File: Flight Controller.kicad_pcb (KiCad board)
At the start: 4 copper layers, 39.5 x 39.5 mm, 123 parts, among them IC1 ICM-20689, IC2 AT7456E, J1 Micro_SD_Card, J2 USB_C_Receptacle_USB2.0_14P, Q1 BC817W, U1 STM32F405RGTx, U2 LMR51430, U3 BMP280, U4 NCP1117-3.3_SOT223

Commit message: Layout Update
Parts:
- moved Rfbb_5R1 19.3 mm to (134.8, 93.5), turned to 180 degrees
- moved Rfbt_5R1 14.3 mm to (134.2, 91.2), turned to 0 degrees
- moved Cin2_5R1 13.0 mm to (139.7, 87.1), turned to -90 degrees
- moved Cin_5R1 12.9 mm to (137.6, 87.1), turned to -90 degrees
- moved Cin3_5R1 12.0 mm to (141.2, 86.3)
- moved C2out_5R1 10.5 mm to (130.1, 82.9), turned to -90 degrees
- moved C1out_5R1 10.3 mm to (128.0, 82.9), turned to -90 degrees
- moved Cboot_5R1 9.77 mm to (132.0, 89.1), turned to 0 degrees
- moved L1 7.42 mm to (134.8, 80.7), turned to 90 degrees
- moved U2 7.19 mm to (134.8, 87.5), turned to -90 degrees
- moved C2_3R1 0.22 mm to (136.5, 74.1)

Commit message: Updated Layout
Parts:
- removed C1_G1: 0.47u, Capacitor_SMD:C_0402_1005Metric
- removed C5: 100n, Capacitor_SMD:C_0402_1005Metric
- removed IC1: ICM-20689, ICM-20689:QFN50P400X400X95-24N
- removed R1, R2: 10k, Resistor_SMD:R_1206_3216Metric
- removed R3_OSD1, R4_OSD1, R5_OSD1: 1k, Resistor_SMD:R_0805_2012Metric
- removed SW_NRST1: SW_Push, Button_Switch_SMD:SW_Tactile_SPST_NO_Straight_CK_PTS636Sx25SMTRLFS
- removed TP_3V1, TP_5V10, TP_5V8, TP_5V9, TP_GND10, TP_GND11, TP_GND12, TP_GND9, TP_Rssi1, TP_S5, TP_S6, TP_VBAT1: TestPoint, Connector:Soldier_Pad
- removed Y_OSD1: 27MHz, Oscillator:Oscillator_SMD_Abracon_ASCO-4Pin_1.6x1.2mm
- added CBOOT_10V1: 0.1u, Capacitor_SMD:C_0402_1005Metric, F.Cu at (202.3, 71.7)
- added CIN_10V1: 4.7u, Capacitor_SMD:C_0805_2012Metric, F.Cu at (203.3, 78.8)
- added CIN_10V2: 4.7u, Capacitor_SMD:C_0805_2012Metric, F.Cu at (203.3, 81.8)
- added CIN_10V3: 0.1u, Capacitor_SMD:C_0402_1005Metric, F.Cu at (202.3, 73.6)
- added COUT_10V1: 22u, Capacitor_SMD:C_0805_2012Metric, F.Cu at (203.3, 84.8)
- added COUT_10V2: 22u, Capacitor_SMD:C_0805_2012Metric, F.Cu at (203.3, 87.9)
- added C_3VG1: 10u, Capacitor_SMD:C_0603_1608Metric_Pad1.08x0.95mm_HandSolder, F.Cu at (203.3, 90.6)
- added C_3VG2: 10u, Capacitor_SMD:C_0603_1608Metric_Pad1.08x0.95mm_HandSolder, F.Cu at (203.3, 93.1)
- added C_VBAT1: 100n, Capacitor_SMD:C_0402_1005Metric, F.Cu at (202.3, 75.6)
- added D6: PESD1CANFD36LS-Q, Diode_SMD:D_SOD-882, F.Cu at (209.6, 75.3)
- added D_LED1: LED, LED_SMD:LED_0603_1608Metric, F.Cu at (207.6, 78.6)
- added D_LED2: LED, LED_SMD:LED_0603_1608Metric, F.Cu at (207.6, 81.2)
- added D_LED3: LED, LED_SMD:LED_0603_1608Metric, F.Cu at (207.6, 83.8)
- added D_LED4: LED, LED_SMD:LED_0603_1608Metric, F.Cu at (207.6, 86.4)
- added L_10V1: 12u, Inductor_SMD:L_Bourns_SRR1208_12.7x12.7mm, F.Cu at (188.6, 70.2)
- added Q2: BC817W, Package_TO_SOT_SMD:SOT-323_SC-70, F.Cu at (206.0, 72.7)
- added RFBB_10V1: 6.2k, Resistor_SMD:R_0805_2012Metric, F.Cu at (183.0, 87.1)
- added RFBT_10V1: 100k, Resistor_SMD:R_1206_3216Metric, F.Cu at (208.3, 89.3)
- added R_BOOT1: 10k, Resistor_SMD:R_0402_1005Metric, F.Cu at (196.1, 85.4)
- added R_BUZ1: 1k, Resistor_SMD:R_0402_1005Metric, F.Cu at (196.1, 87.3)
- added R_CC1: 220, Resistor_SMD:R_0402_1005Metric, F.Cu at (196.1, 89.3)
- added R_FLASH1: 10K, Resistor_SMD:R_0402_1005Metric, F.Cu at (196.1, 91.3)
- added R_FLASH2: 10K, Resistor_SMD:R_0402_1005Metric, F.Cu at (196.1, 93.3)
- added R_LED1: 1k, Resistor_SMD:R_0603_1608Metric, F.Cu at (192.6, 85.6)
- added R_LED2: 1k, Resistor_SMD:R_0603_1608Metric, F.Cu at (192.6, 88.1)
- added R_LED3: 1k, Resistor_SMD:R_0603_1608Metric, F.Cu at (192.6, 90.6)
- added R_LED4: 1k, Resistor_SMD:R_0603_1608Metric, F.Cu at (192.6, 93.2)
- added R_VBAT1: 100K, Resistor_SMD:R_0805_2012Metric, F.Cu at (183.0, 90.1)
- added R_VBAT2: 10K, Resistor_SMD:R_1206_3216Metric, F.Cu at (208.3, 92.7)
- added TP_VBAT+2: TestPoint, TestPoint:TestPoint_Pad_D2.5mm, F.Cu at (198.6, 73.0)
- added U5: LMR51430, Package_TO_SOT_SMD:SOT-23-6, F.Cu at (187.7, 88.0)
- added U6: W25Q128JVSIQ TR, footprints:SOIC_208MIL_WIN, F.Cu at (195.8, 80.8)
- added U7: ICM-42688-P, Package_LGA:Bosch_LGA-14_3x2.5mm_P0.5mm, F.Cu at (187.7, 92.5)
- added U8: NCP1117-3.3_SOT223, Package_TO_SOT_SMD:SOT-223-3_TabPin2, F.Cu at (185.7, 81.5)
- added Y2: 27M, AWSCR-27.00CV-T :E2X270061X04, F.Cu at (210.1, 72.4)
- C_3V1: renamed from C1_3R1; footprint Capacitor_SMD:C_0805_2012Metric -> Capacitor_SMD:C_0603_1608Metric
- C_3V2: renamed from C2_3R1; footprint Capacitor_SMD:C_0805_2012Metric -> Capacitor_SMD:C_0603_1608Metric
- C_DEC1: renamed from C1_Dec1; footprint Capacitor_SMD:C_0805_2012Metric -> Capacitor_SMD:C_0603_1608Metric
- C_GYRO1: renamed from C3_G1; footprint Capacitor_SMD:C_0805_2012Metric -> Capacitor_SMD:C_0402_1005Metric
- C_OSD2: renamed from C2_OSD1; footprint Capacitor_SMD:C_0805_2012Metric -> Capacitor_SMD:C_0402_1005Metric
- C_OSD3: renamed from C3_OSD1; footprint Capacitor_SMD:C_0805_2012Metric -> Capacitor_SMD:C_0402_1005Metric
- D_LED5: renamed from D1_LED1; footprint LED_SMD:LED_0402_1005Metric -> LED_SMD:LED_0603_1608Metric
- D_LED6: renamed from D2_LED1; footprint LED_SMD:LED_0402_1005Metric -> LED_SMD:LED_0603_1608Metric
- IC2: footprint MAX7456EUI:SOP65P637X110-28N -> max74:SOP65P637X110-28N
- J1: value Micro_SD_Card -> Conn_01x08_MountingPin; footprint Connector_Card:microSD_HC_Molex_47219-2001 -> Connector_JST:JST_SH_SM08B-SRSS-TB_1x08-1MP_P1.00mm_Horizontal; moved to F.Cu
- J2: footprint Connector_USB:USB_C_Receptacle_HRO_TYPE-C-31-M-12 -> Connector_USB:USB_C_Receptacle_GCT_USB4110
- JP1: value SolderJumper_3_Open -> Jumper_3
- L_5V1: renamed from L1; value 6.8u -> 8.2u; footprint Inductor_SMD:L_Abracon_ASPI-0630LR -> Inductor_SMD:L_Vishay_IHLP-2525
- R_I2C1: renamed from R3_I2C1; footprint Resistor_SMD:R_0603_1608Metric -> Resistor_SMD:R_0402_1005Metric
- R_I2C2: renamed from R3_I2C2; footprint Resistor_SMD:R_0603_1608Metric -> Resistor_SMD:R_0402_1005Metric
- R_LED5: renamed from R1_LED1; footprint Resistor_SMD:R_0805_2012Metric -> Resistor_SMD:R_0603_1608Metric
- R_LED6: renamed from R2_LED1; footprint Resistor_SMD:R_0805_2012Metric -> Resistor_SMD:R_0603_1608Metric
- R_SBUS2: renamed from R1_SBUS1; footprint Resistor_SMD:R_1206_3216Metric -> Resistor_SMD:R_0603_1608Metric
- U1: value STM32F405RGTx -> AT32F435RGT7
- Y1: renamed from 8M1; value Resonator -> 8M
- moved J1 65.4 mm to (202.8, 66.9), turned to 0 degrees
- renumbered Cboot_5R1 to CBOOT_5V1, Cin_5R1 to CIN_5V1, Cin2_5R1 to CIN_5V2, Cin3_5R1 to CIN_5V3, C1out_5R1 to COUT_5V1, C2out_5R1 to COUT_5V2, C3 to C_BARO1, C4 to C_BARO2, C2_Dec1 to C_DEC2, C3_Dec1 to C_DEC3, C4_Dec1 to C_DEC4, C5_Dec1 to C_DEC5, C6_Dec1 to C_DEC6, C7_Dec1 to C_DEC7, C4_G1 to C_GYRO2, C2_G1 to C_GYRO3, C1_OSD1 to C_OSD1, C4_OSD1 to C_OSD4, C5_OSD1 to C_OSD5, C6_OSD1 to C_OSD6, Q1 to Q_SBUS1, Rfbb_5R1 to RFBB_5V1, Rfbt_5R1 to RFBT_5V1, R1_OSD1 to R_OSD1, R2_OSD1 to R_OSD2, R2_SBUS1 to R_SBUS1, R4_USB2 to R_USB1, R3_USB2 to R_USB2, TP_SBUS1 to TP_RX1, TP_TX1 to TP_SBUS1
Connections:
- net Net-(U1-PH0) renamed /RES1
- net Net-(U1-PH1) renamed /RES2
- net Net-(U1-VCAP_1) renamed /CAP1
- net Net-(U1-VCAP_2) renamed /CAP2
- net Net-(U4-VI) renamed /5V_OUT
- CIN_5V1 pad 2: Net-(U2-GND) -> GND
- CIN_5V2 pad 2: Net-(U2-GND) -> GND
- CIN_5V3 pad 1: Net-(U2-GND) -> GND
- COUT_5V1 pad 2: Net-(U2-GND) -> GND
- COUT_5V2 pad 2: Net-(U2-GND) -> GND
- C_GYRO3 pad 1: +3.3V -> +3.3V_GYRO
- IC2 pad 10: /SPI2_SCLK -> /OSD_SCLK
- IC2 pad 11: /SPI2_MISO -> /OSD_MISO
- IC2 pad 12: /LOS -> unconnected-(IC2-LOS-Pad12)
- IC2 pad 17: /VS -> unconnected-(IC2-~{VSYNC}-Pad17)
- IC2 pad 18: /HS -> unconnected-(IC2-~{HSYNC}-Pad18)
- IC2 pad 7: /CLKOUT -> unconnected-(IC2-CLKOUT-Pad7)
- IC2 pad 9: /SPI2_MOSI -> /OSD_MOSI
- J1 pad 1: unconnected-(J1-DAT2-Pad1) -> /VBAT+
- J1 pad 2: /SD_CS -> GND
- J1 pad 3: /SPI2_MOSI -> /S1
- J1 pad 4: +3.3V -> /S2
- J1 pad 5: /SPI2_SCLK -> /S3
- J1 pad 6: GND -> /S4
- J1 pad 7: /SPI2_MISO -> /ADC_Curr
- J1 pad 8: unconnected-(J1-DAT1-Pad8) -> /TEL
- RFBB_5V1 pad 2: Net-(U2-GND) -> GND
- R_I2C1 pad 2: /I2C_SDA -> /I2C2_SDA
- R_I2C2 pad 1: /I2C_SCL -> /I2C2_SCL
- R_LED5 pad 2: /LED1 -> /LED0
- R_LED6 pad 2: /LED2 -> /LED1
- TP_Buz1 pad 1: /Buz -> /BUZ-
- TP_Curr1 pad 1: /Curr -> /ADC_Curr
- TP_GND5 pad 1: GND -> +5V
- TP_LED1 pad 1: /LED_Out -> /LED_S
- TP_S2 pad 1: /S2 -> /S3
- TP_S3 pad 1: /S3 -> /S2
- TP_SCL1 pad 1: /I2C_SCL -> /I2C2_SCL
- TP_SDA1 pad 1: /I2C_SDA -> /I2C2_SDA
- U1 pad 10: /SPI2_MISO -> unconnected-(U1-PC2-Pad10)
- U1 pad 11: /SPI2_MOSI -> /ADC_Curr
- U1 pad 14: /Curr -> /UART4_TX
- U1 pad 15: /Rssi -> /UART4_RX
- U1 pad 2: unconnected-(U1-PC13-Pad2) -> /BUZ
- U1 pad 20: /VBAT+ -> /GYRO_CS
- U1 pad 21: /SPI1_SCLK -> /OSD_SCLK
- U1 pad 22: /SPI1_MISO -> /OSD_MISO
- U1 pad 23: /SPI1_MOSI -> /OSD_MOSI
- U1 pad 24: /INT -> /GYRO_INT
- U1 pad 25: Net-(U1-PC5) -> unconnected-(U1-PC5-Pad25)
- U1 pad 26: /OSD_CS -> /LED0
- U1 pad 27: /SD_CS -> /LED1
- U1 pad 29: /UART3_TX -> /I2C2_SCL
- U1 pad 30: /UART3_RX -> /I2C2_SDA
- U1 pad 33: unconnected-(U1-PB12-Pad33) -> /FLASH_CS
- U1 pad 34: /SPI2_SCLK -> /GYRO_SCLK
- U1 pad 35: unconnected-(U1-PB14-Pad35) -> /GYRO_MISO
- U1 pad 36: unconnected-(U1-PB15-Pad36) -> /GYRO_MOSI
- U1 pad 37: /S3 -> /S1
- U1 pad 38: /S4 -> /S2
- U1 pad 39: /S5 -> /S3
- U1 pad 40: /S6 -> /S4
- U1 pad 41: /S1 -> /LED_S
- U1 pad 42: /S2 -> /CC
- U1 pad 43: /UART1_RX -> unconnected-(U1-PA10-Pad43)
- U1 pad 46: unconnected-(U1-PA13-Pad46) -> /SWD
- U1 pad 49: unconnected-(U1-PA14-Pad49) -> /SWC
- U1 pad 50: /Buz -> /OSD_CS
- U1 pad 51: /UART4_TX -> /UART3_TX
- U1 pad 52: /UART4_RX -> /UART3_RX
- U1 pad 55: /LED_Out -> /FLASH_SCLK
- U1 pad 56: /LED1 -> /FLASH_MISO
- U1 pad 57: /LED2 -> /FLASH_MOSI
- U1 pad 59: /I2C_SDA -> /UART1_RX
- U1 pad 60: Net-(JP1-C) -> /BOOT
- U1 pad 61: /I2C_SCL -> /BARO_SCL
- U1 pad 62: unconnected-(U1-PB9-Pad62) -> /BARO_SDA
- U1 pad 7: Net-(U1-NRST) -> unconnected-(U1-NRST-Pad7)
- U1 pad 8: /Baro_CS -> unconnected-(U1-PC0-Pad8)
- U1 pad 9: /Gyro_CS -> /ADC_VBAT
- U2 pad 1: Net-(U2-GND) -> GND
- U3 pad 2: /Baro_CS -> +3.3V
- U3 pad 3: /SPI1_MOSI -> /BARO_SDA
- U3 pad 4: /SPI1_SCLK -> /BARO_SCL
- U3 pad 5: /SPI1_MISO -> GND

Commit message: First Layout
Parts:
- CBOOT_10V1, CBOOT_5V1: footprint Capacitor_SMD:C_0402_1005Metric -> Capacitor_SMD:C_0603_1608Metric
- C_3VG1, C_3VG2, J1, R_FLASH1, R_FLASH2, R_LED1, R_LED2, R_LED3, R_LED4, R_LED5, R_LED6, U6, U8, Y2: moved to B.Cu
- L_10V1: footprint Inductor_SMD:L_Bourns_SRR1208_12.7x12.7mm -> Wurth-Elektronik:744393465120
- RFBB_10V1, RFBB_5V1: footprint Resistor_SMD:R_0805_2012Metric -> Resistor_SMD:R_0402_1005Metric
- RFBT_10V1, RFBT_5V1: footprint Resistor_SMD:R_1206_3216Metric -> Resistor_SMD:R_0402_1005Metric
- moved D_LED4 73.1 mm to (134.5, 83.5), turned to 180 degrees
- moved D_LED3 73.1 mm to (134.5, 81.8), turned to 180 degrees
- moved D_LED2 73.1 mm to (134.5, 80.0), turned to 180 degrees
- moved D_LED1 73.0 mm to (134.5, 78.2), turned to 180 degrees
- moved COUT_10V1 73.0 mm to (130.3, 85.8)
- moved COUT_10V2 73.0 mm to (130.3, 87.8)
- moved CIN_10V3 70.9 mm to (135.2, 96.7), turned to 180 degrees
- moved RFBT_10V1 69.3 mm to (139.0, 90.6), turned to -90 degrees
- moved CIN_10V1 68.9 mm to (135.8, 92.9)
- moved CIN_10V2 68.8 mm to (135.8, 95.0)
- moved J1 68.0 mm to (144.2, 101.5), turned to 180 degrees
- moved CBOOT_10V1 67.3 mm to (136.9, 87.5), turned to 180 degrees
- moved R_FLASH1 66.3 mm to (133.7, 69.0), turned to -90 degrees
- moved Y2 64.0 mm to (151.0, 96.9), turned to 180 degrees
- moved R_LED4 63.2 mm to (130.2, 83.5)
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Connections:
- D2 pad 1: +5V -> /5V_USB
- D2 pad 2: /5V_USB -> +5V

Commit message: Updated Layout
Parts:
- removed TP_3V2, TP_5V1, TP_5V11, TP_5V12, TP_5V2, TP_5V3, TP_5V4, TP_5V5, TP_5V6, TP_5V7, TP_Buz1, TP_CAM1, TP_Curr1, TP_GND1, TP_GND2, TP_GND3, TP_GND4, TP_LED1, TP_VTX1: TestPoint, Connector:Soldier_Pad
- removed TP_VBAT-1: TestPoint, TestPoint:TestPoint_Pad_D2.5mm
- added 10V: TestPoint, Pads:Solder_Pad_SMD, F.Cu at (134.6, 99.3)
- added 3V: TestPoint, Pads:Solder_Pad_SMD, F.Cu at (136.5, 99.3)
- added 3V: TestPoint, Pads:Solder_Pad_SMD, F.Cu at (138.4, 99.3)
- added 5V: TestPoint, Pads:Solder_Pad_SMD, F.Cu at (147.9, 99.3)
- added 5V: TestPoint, Pads:Solder_Pad_SMD, F.Cu at (144.1, 99.3)
- added 5V: TestPoint, Pads:Solder_Pad_SMD, F.Cu at (149.8, 99.3)
- added 5V: TestPoint, Pads:Solder_Pad_SMD, F.Cu at (134.9, 124.8)
- added 5V: TestPoint, Pads:Solder_Pad_SMD, F.Cu at (140.3, 99.3)
- added 5V: TestPoint, Pads:Solder_Pad_SMD, F.Cu at (137.5, 102.9)
- added 5V: TestPoint, Pads:Solder_Pad_SMD, F.Cu at (142.2, 99.3)
- added 5V: TestPoint, Pads:Solder_Pad_SMD, F.Cu at (151.7, 99.3)
- added 5V: TestPoint, Pads:Solder_Pad_SMD, F.Cu at (135.6, 102.9)
- added 5V: TestPoint, Pads:Solder_Pad_SMD, F.Cu at (146.0, 99.3)
- added Buz: TestPoint, Pads:Solder_Pad_SMD, F.Cu at (139.4, 102.9)
- added CAM: TestPoint, Pads:Solder_Pad_SMD, F.Cu at (141.3, 102.9)
- added CC: TestPoint, Pads:Solder_Pad_SMD, F.Cu at (143.2, 102.9)
- added Curr: TestPoint, Pads:Solder_Pad_SMD, F.Cu at (145.1, 102.9)
- added G***: LOGO, Pads:OpenSource_Logo, F.Cu at (141.3, 94.9)
- added G***: LOGO, Pads:FAFO_LOGO, F.Cu at (160.1, 95.3)
- added G***: LOGO, Pads:OpenSource_Text, F.Cu at (147.6, 95.7)
- added GND: TestPoint, Pads:Solder_Pad_SMD, F.Cu at (147.0, 102.9)
- added GND: TestPoint, Pads:Solder_Pad_SMD, F.Cu at (153.6, 99.3)
- added GND: TestPoint, Pads:Solder_Pad_SMD, F.Cu at (150.8, 102.9)
- added GND: TestPoint, Pads:Solder_Pad_SMD, F.Cu at (148.9, 102.9)
- added LED: TestPoint, Pads:Solder_Pad_SMD, F.Cu at (152.7, 102.9)
- added TEL: TestPoint, Pads:Solder_Pad_SMD, F.Cu at (154.6, 102.9)
- added TP_GND10: TestPoint, Pads:Solder_Pad_SMD, F.Cu at (143.3, 67.5)
- added TP_GND15: TestPoint, Pads:Solder_Pad_SMD, F.Cu at (149.0, 67.5)
- added TP_GND9: TestPoint, Pads:Solder_Pad_SMD, F.Cu at (141.4, 67.5)
- added TP_S5: TestPoint, Pads:Solder_Pad_SMD, F.Cu at (150.9, 67.5)
- added TP_S6: TestPoint, Pads:Solder_Pad_SMD, F.Cu at (152.8, 67.5)
- added TP_S7: TestPoint, Pads:Solder_Pad_SMD, F.Cu at (146.5, 133.0)
- added TP_S8: TestPoint, Pads:Solder_Pad_SMD, F.Cu at (148.4, 133.0)
- added TP_SWC1: TestPoint, Pads:Solder_Pad_SMD, F.Cu at (174.4, 129.3)
- added TP_SWD1: TestPoint, Pads:Solder_Pad_SMD, F.Cu at (154.7, 67.5)
- added TP_TX1: TestPoint, Pads:Solder_Pad_SMD, F.Cu at (151.8, 71.0)
- added VBAT: TestPoint, Pads:Solder_Pad_SMD, F.Cu at (161.2, 126.4)
- added VTX: TestPoint, Pads:Solder_Pad_SMD, F.Cu at (155.5, 99.3)
- C_DEC1, D6: moved to B.Cu
- FC 1: renamed from D_LED5
- FC 2: renamed from D_LED6
- TP_GND13, TP_GND14, TP_GND5, TP_GND6, TP_GND7, TP_GND8, TP_RX1, TP_RX2, TP_RX3, TP_RX4, TP_RX5, TP_S1, TP_S2, TP_S3, TP_S4, TP_SBUS1, TP_SCL1, TP_SDA1, TP_TX2, TP_TX3, TP_TX4, TP_TX5: footprint Connector:Soldier_Pad -> Pads:Solder_Pad_SMD
- TP_VBAT+1, TP_VBAT+2: footprint TestPoint:TestPoint_Pad_D2.5mm -> Pads:Solder_Pad_SMD
- moved TP_SBUS1 159.8 mm to (150.3, 133.0)
- moved TP_TX4 153.9 mm to (148.4, 136.8)
- moved TP_GND5 153.3 mm to (145.6, 126.7)
- moved TP_TX3 147.6 mm to (146.5, 136.8)
- moved TP_SDA1 137.7 mm to (155.6, 71.0)
- moved TP_S4 127.0 mm to (149.9, 71.0)
- moved TP_GND6 124.7 mm to (135.7, 67.5)
- moved TP_TX2 121.2 mm to (153.7, 71.0)
- moved TP_GND13 119.7 mm to (145.2, 67.5)
- moved TP_S1 118.9 mm to (144.2, 71.0)
- moved TP_GND14 118.6 mm to (147.1, 67.5)
- moved TP_S2 115.9 mm to (146.1, 71.0)
- moved TP_S3 111.8 mm to (148.0, 71.0)
- moved R_BUZ1 110.2 mm to (135.3, 75.0), turned to 90 degrees
- moved Q2 109.2 mm to (137.8, 74.0)
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- renumbered D_LED2 to 10V, D_LED3 to 3.3V, D_LED1 to 5V, D_LED4 to Gyro

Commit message: Updated Layout
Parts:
- removed 10V, 3V (x2), 5V (x10), Buz, CAM, CC, Curr, GND (x4), LED, TEL, TP_GND10, TP_GND13, TP_GND14, TP_GND15, TP_GND5, TP_GND6, TP_GND7, TP_GND8, TP_GND9, TP_RX1, TP_RX2, TP_RX3, TP_RX4, TP_RX5, TP_S1, TP_S2, TP_S3, TP_S4, TP_S5, TP_S6, TP_S7, TP_S8, TP_SBUS1, TP_SCL1, TP_SDA1, TP_SWC1, TP_SWD1, TP_TX1, TP_TX2, TP_TX3, TP_TX4, TP_TX5, TP_VBAT+1, TP_VBAT+2, VBAT, VTX: TestPoint, Pads:Solder_Pad_SMD
- D_LED5: renamed from FC 1
- D_LED6: renamed from FC 2
- moved R_I2C1 17.4 mm to (148.5, 93.5), turned to 90 degrees
- moved R_I2C2 17.3 mm to (147.4, 93.5), turned to -90 degrees
- moved R_VBAT1 12.4 mm to (138.8, 94.1), turned to -90 degrees
- moved R_VBAT2 12.1 mm to (141.0, 94.7), turned to -90 degrees
- moved C_VBAT1 11.9 mm to (142.7, 95.5), turned to 90 degrees
- moved D2 4.47 mm to (146.3, 82.8)
- moved R_USB2 2.15 mm to (158.6, 75.9)
- moved C_DEC6 1.93 mm to (138.3, 80.2)
- moved C_DEC7 1.93 mm to (154.5, 80.9), turned to 0 degrees
- moved C1 1.70 mm to (149.9, 92.9)
- moved R_LED1 1.48 mm to (128.7, 78.0)
- moved R_LED2 1.48 mm to (128.7, 79.8)
- moved R_LED3 1.48 mm to (128.7, 81.5)
- moved R_LED4 1.48 mm to (128.7, 83.2)
- moved R_LED5 1.48 mm to (128.7, 74.5)
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- renumbered 5V to D_LED1, 10V to D_LED2, 3.3V to D_LED3, Gyro to D_LED4
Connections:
- U1 pad 26: /LED0 -> /LED1
- U1 pad 27: /LED1 -> /LED0

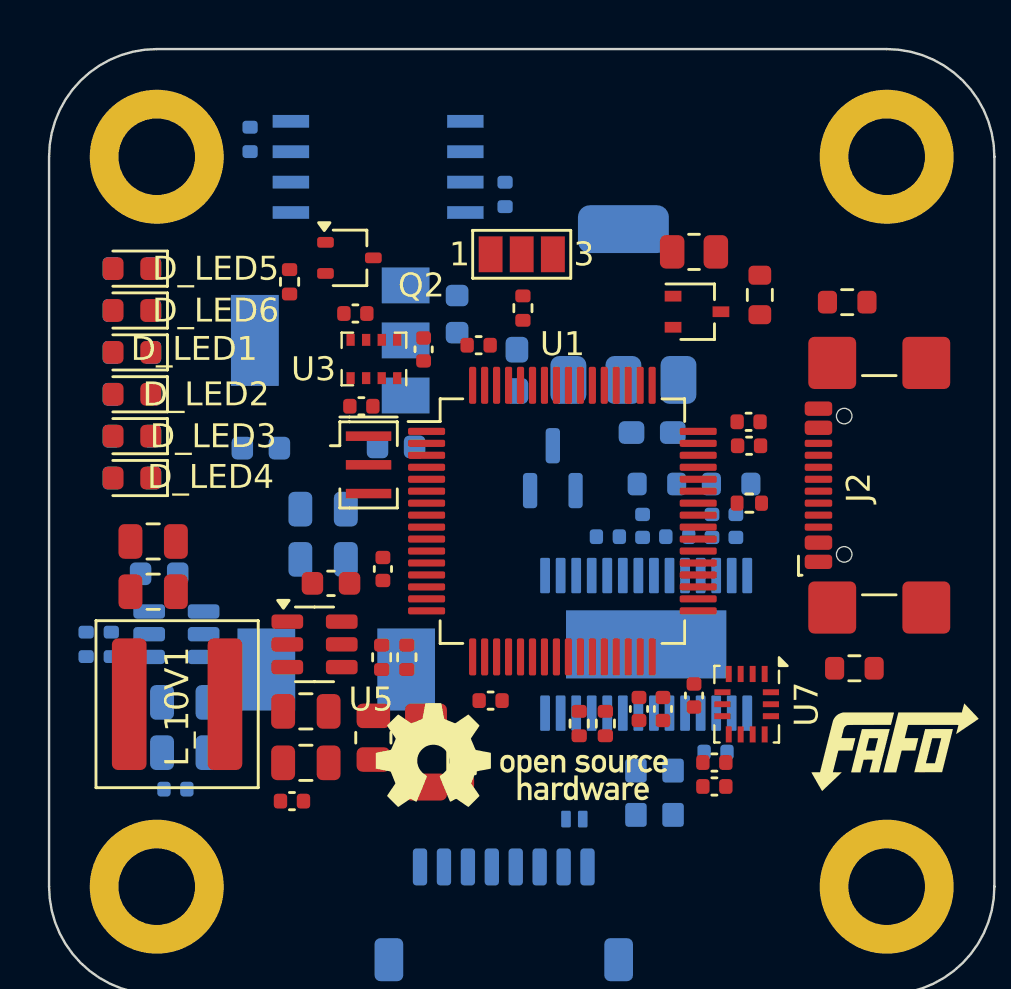
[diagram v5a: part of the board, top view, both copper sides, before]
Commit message: Changed LDOs
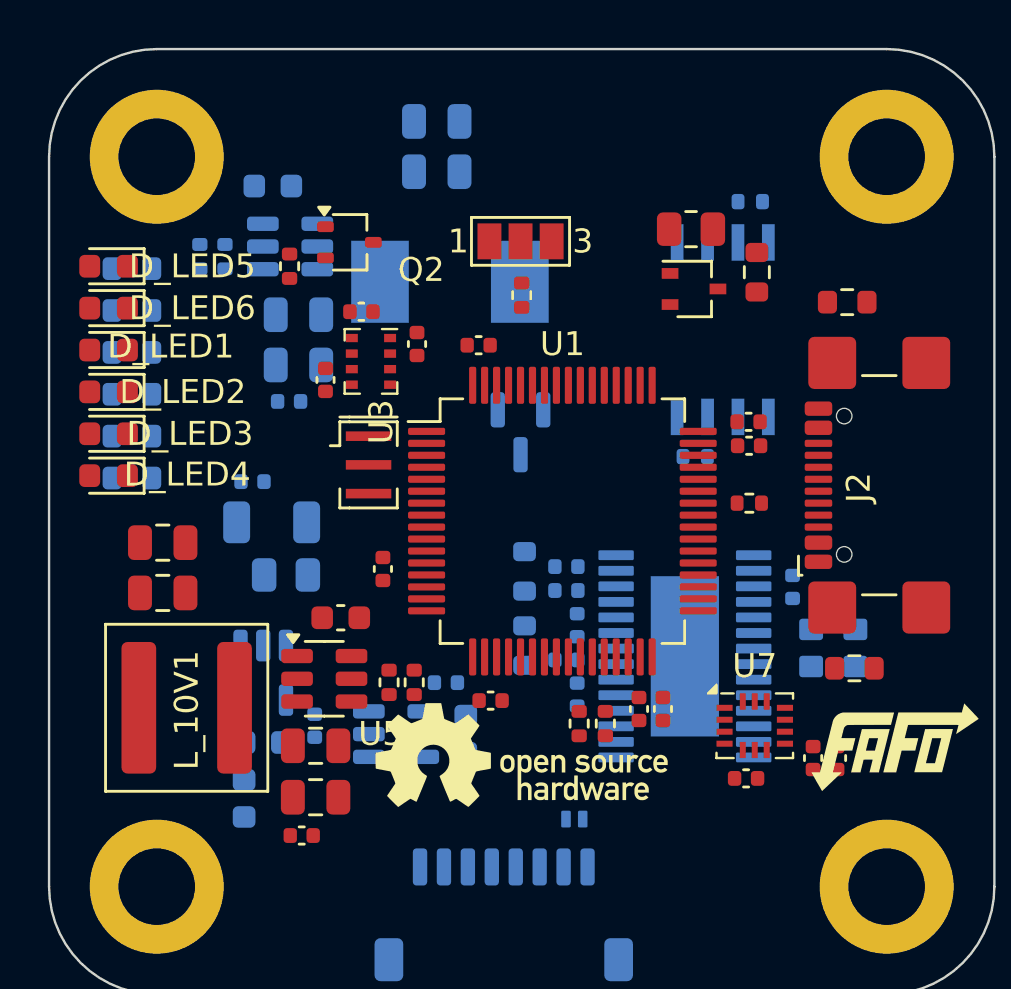
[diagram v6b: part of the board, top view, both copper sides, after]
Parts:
- removed the C_3VG1 at (144.8, 78.8)
- added C_3VG2: 10n, Capacitor_SMD:C_0402_1005Metric, B.Cu at (141.8, 91.8)
- C_3V1: value 10u -> 1u
- C_3V2: value 10u -> 10n; footprint Capacitor_SMD:C_0603_1608Metric -> Capacitor_SMD:C_0402_1005Metric
- C_3VG1: renamed from C_3VG2; value 10u -> 1u; footprint Capacitor_SMD:C_0603_1608Metric_Pad1.08x0.95mm_HandSolder -> Capacitor_SMD:C_0603_1608Metric
- C_VBAT1, R_VBAT1, R_VBAT2: moved to B.Cu
- U4, U8: value NCP1117-3.3_SOT223 -> SPX3819M5-L-3-3; footprint Package_TO_SOT_SMD:SOT-223-3_TabPin2 -> Package_TO_SOT_SMD:SOT-23-5
- moved R_FLASH1 21.1 mm to (154.6, 71.7), turned to 180 degrees
- moved U8 20.3 mm to (139.8, 94.0), turned to 0 degrees
- moved C_3V2 18.2 mm to (136.3, 93.6), turned to -90 degrees
- moved RFBB_5V1 16.9 mm to (131.6, 74.0)
- moved CBOOT_5V1 16.9 mm to (134.6, 71.0)
- moved CIN_5V1 16.9 mm to (135.7, 76.4)
- moved CIN_5V3 16.9 mm to (135.3, 80.0)
- moved COUT_5V1 16.9 mm to (141.4, 68.3)
- moved COUT_5V2 16.9 mm to (141.4, 70.5)
- moved L_5V1 16.9 mm to (142.0, 75.0)
- moved RFBT_5V1 16.9 mm to (132.6, 74.0)
- moved U2 16.9 mm to (135.3, 73.6)
- moved CIN_5V2 16.9 mm to (135.7, 78.5)
- moved U6 15.9 mm to (153.4, 77.0), turned to -90 degrees
- moved C_VBAT1 15.1 mm to (133.8, 83.4), turned to 0 degrees
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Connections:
- C_3V1 pad 1: /5V_OUT -> +3.3V
- C_3V2 pad 1: +3.3V -> Net-(U4-BP)
- D2 pad 1: /5V_USB -> +5V
- D2 pad 2: +5V -> /5V_USB
- U4 pad 1: GND -> /5V_OUT
- U4 pad 2: +3.3V -> GND
- U8 pad 1: GND -> /5V_OUT
- U8 pad 2: +3.3V_GYRO -> GND

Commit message: Routing
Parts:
- moved G*** 26.1 mm to (135.8, 86.5)
- moved C_OSD1 8.93 mm to (147.6, 85.8)
- moved C_OSD2 8.93 mm to (138.2, 85.0)
- moved C_OSD3 8.93 mm to (138.2, 86.0)
- moved C_OSD4 8.93 mm to (138.6, 87.5)
- moved C_OSD6 8.93 mm to (138.6, 90.3)
- moved IC2 8.93 mm to (143.1, 88.8)
- moved R_OSD1 8.93 mm to (136.4, 85.2)
- moved R_OSD2 8.93 mm to (136.4, 88.3)
- moved C_OSD5 8.93 mm to (138.2, 88.9)
- moved Y2 8.26 mm to (150.3, 87.4)
- moved C_3V1 4.76 mm to (129.4, 94.6)
- moved C_3V2 4.76 mm to (131.6, 93.9)
- moved C_3VG1 4.76 mm to (137.9, 94.2)
- moved C_3VG2 4.76 mm to (137.1, 92.1)
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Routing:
- net /FLASH_CS: track 0.00 -> 33.4 mm, vias 0 -> 1
- net /OSD_MISO: track 0.00 -> 19.3 mm, vias 0 -> 3
- net /OSD_SCLK: track 0.00 -> 18.6 mm, vias 0 -> 3
- net +3.3V: track 0.00 -> 16.7 mm
- net GND: track 0.00 -> 16.4 mm
- net /GYRO_CS: track 0.00 -> 15.1 mm, vias 0 -> 2
- net /BUZ: track 0.00 -> 14.4 mm, vias 0 -> 2
- net /FLASH_MOSI: track 0.00 -> 14.1 mm, vias 0 -> 1
- net /FLASH_MISO: track 0.00 -> 13.6 mm, vias 0 -> 1
- net /UART1_TX: track 0.00 -> 12.4 mm
- net /OSD_CS: track 0.00 -> 12.1 mm, vias 0 -> 1
- net /FLASH_SCLK: track 0.00 -> 11.2 mm, vias 0 -> 1
- net /GYRO_INT: track 0.00 -> 10.7 mm
- net /GYRO_MISO: track 0.00 -> 9.42 mm, vias 0 -> 2
- net /GYRO_MOSI: track 0.00 -> 8.84 mm, vias 0 -> 2
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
